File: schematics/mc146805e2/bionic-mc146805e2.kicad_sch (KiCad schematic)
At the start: 5 parts, among them J1 Bionic-P135, J2 Bionic-P245, U1 MC146805E2P, U3 11AA010-I/TO

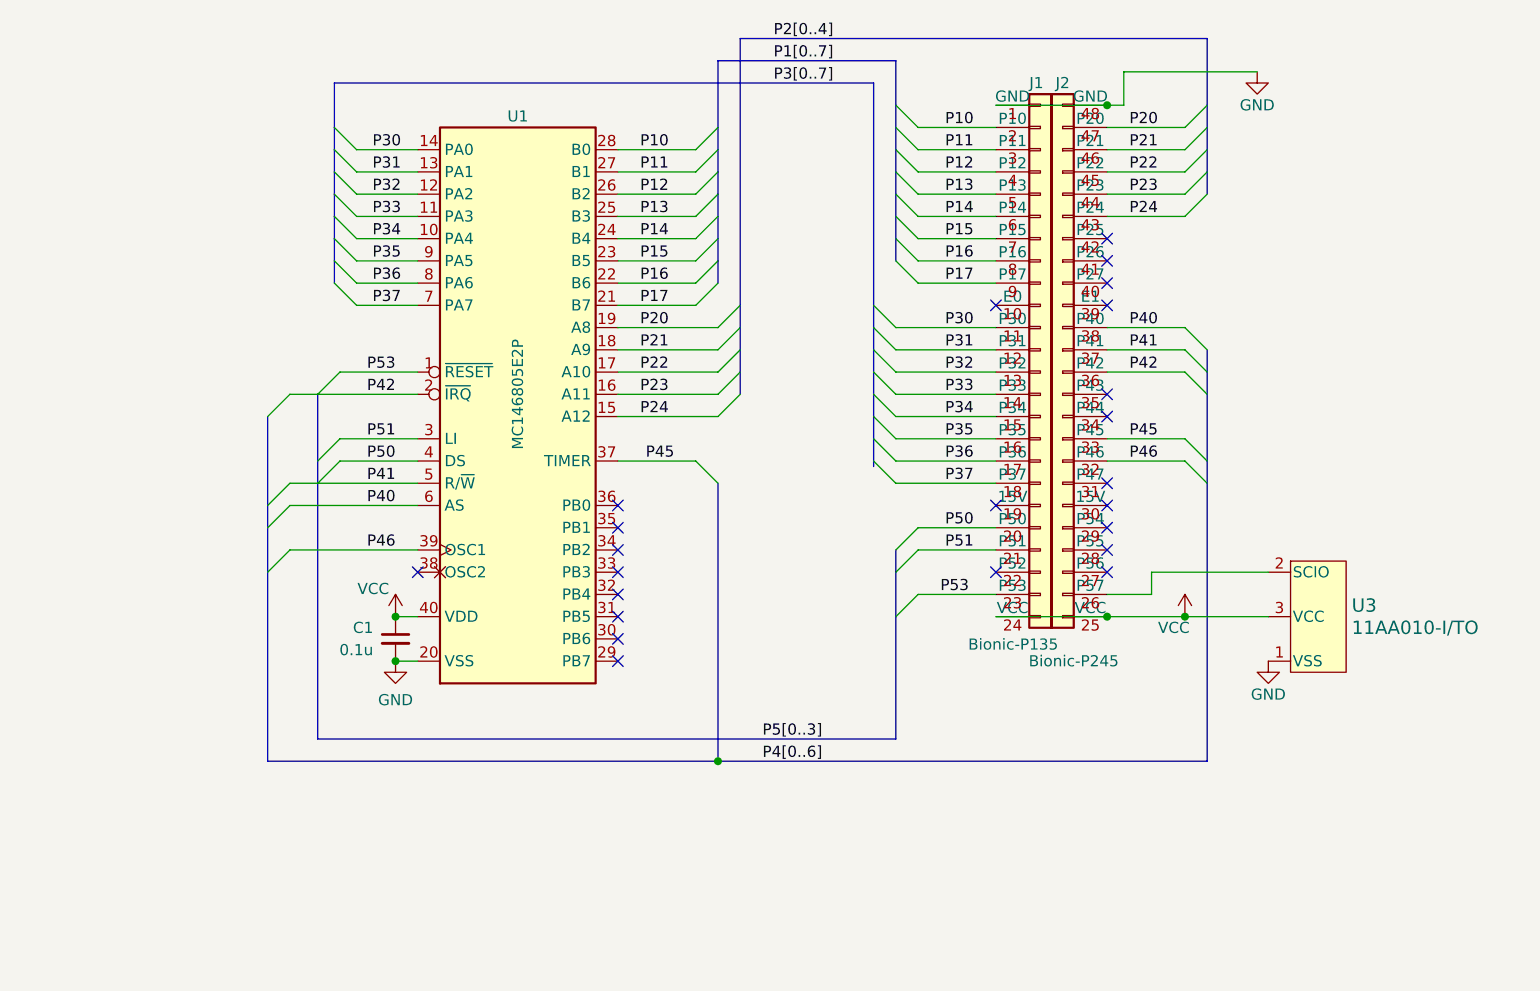
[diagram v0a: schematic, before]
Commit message: [schematics] Make board edges round
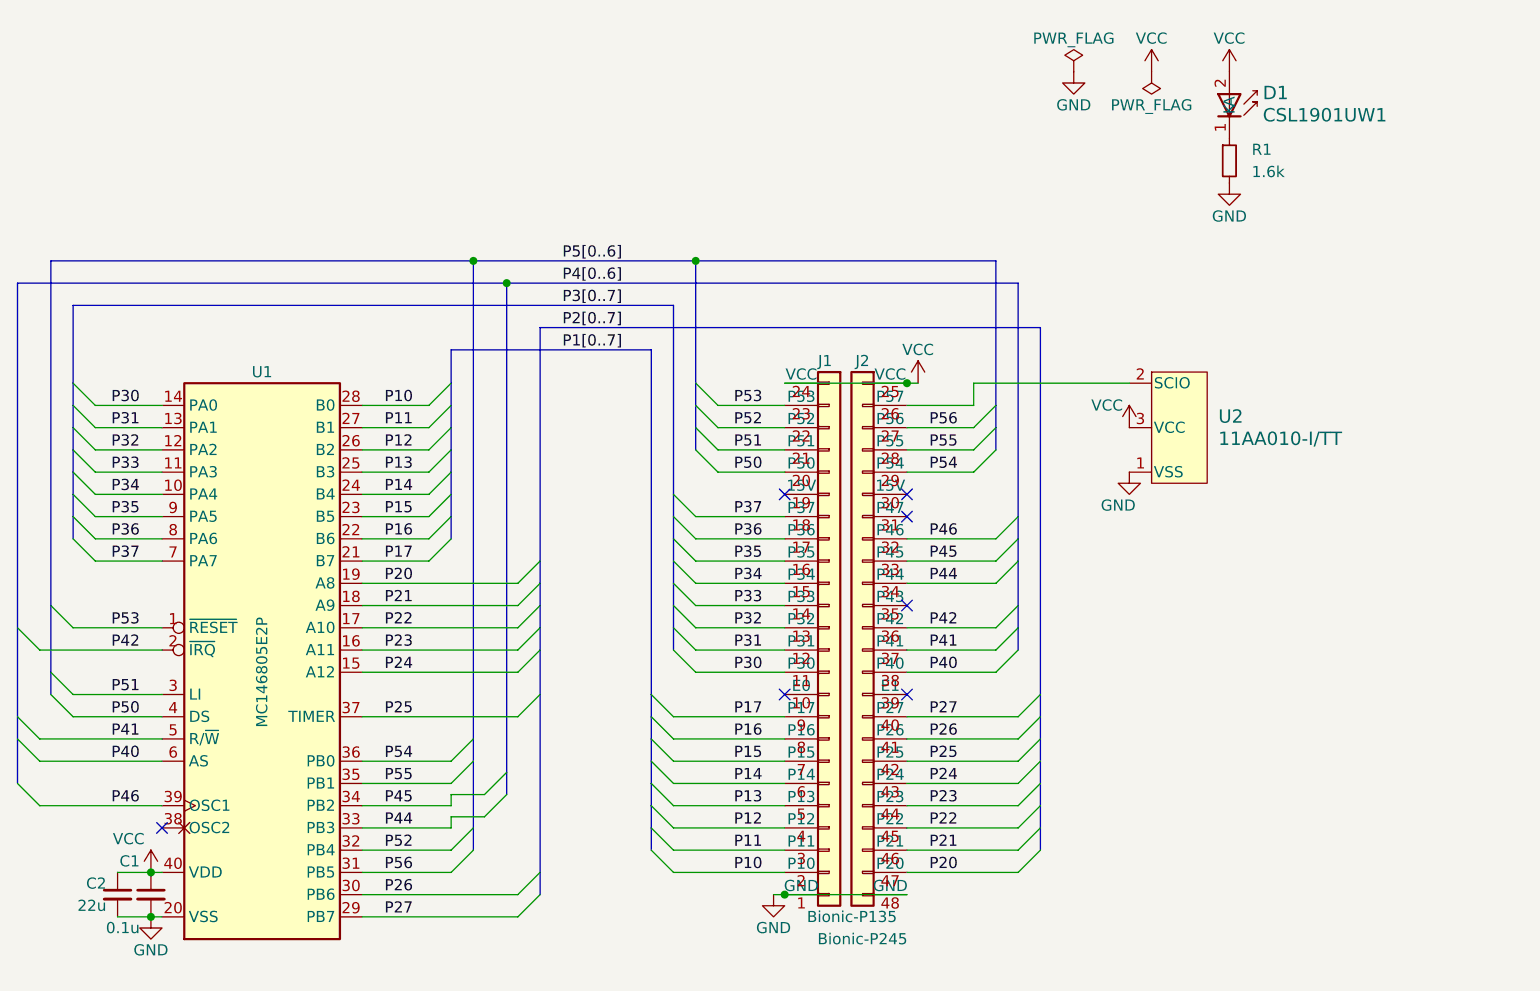
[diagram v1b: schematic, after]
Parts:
- removed U3: 11AA010-I/TO, TO-92_MC_MCH, symbol 0-LocalLibrary:11AA010-I_TO
- added C2: 22u, Capacitor_SMD:C_0603_1608Metric_Pad1.08x0.95mm_HandSolder, symbol Device:C_Small
- added D1: CSL1901UW1, 0-LocalLibrary:LED_CSL1901UW1_ROM, symbol 0-LocalLibrary:CSL1901UW1
- added R1: 1.6k, Resistor_SMD:R_0603_1608Metric_Pad0.98x0.95mm_HandSolder, symbol Device:R_Small
- added U2: 11AA010-I/TT, 0-LocalLibrary:SOT-23_MC_MCH-M, symbol 0-LocalLibrary:11AA010-I_TT
- C1: footprint Capacitor_THT:C_Disc_D3.4mm_W2.1mm_P2.50mm -> Capacitor_SMD:C_0603_1608Metric_Pad1.08x0.95mm_HandSolder
- U1: footprint Package_DIP:DIP-40_W15.24mm -> 0-LocalLibrary:DIP-40_W15.24mm_Socket
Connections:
- net GND: now also C2.2, R1.2, U2.1 (VSS)
- net P45: now also U1.34 (PB2); no longer U1.37 (TIMER)
- net VCC: now also C2.1, D1.2 (A), U2.3 (VCC)
- net P27: now reaches U1.29 (PB7)
- net P27: now also J2.40 (P27)
- net P26: now reaches U1.30 (PB6)
- net P26: now also J2.41 (P26)
- net P56: now reaches U1.31 (PB5)
- net P56: now also J2.27 (P56)
- net P52: now reaches U1.32 (PB4)
- net P52: now also J1.22 (P52)
- net P44: now reaches U1.33 (PB3)
- net P44: now also J2.34 (P44)
- net P55: now reaches U1.35 (PB1)
- net P55: now also J2.28 (P55)
- net P54: now reaches U1.36 (PB0)
- net P54: now also J2.29 (P54)
- net at J2.26 (P57): now also U2.2 (SCIO)
- net P25: now reaches J2.42 (P25)
- net P25: now also U1.37 (TIMER)
- new net: D1.1 (K), R1.1
- no-connect marks 23 -> 7

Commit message: [MC146805E2] Fix EEPROM pinout
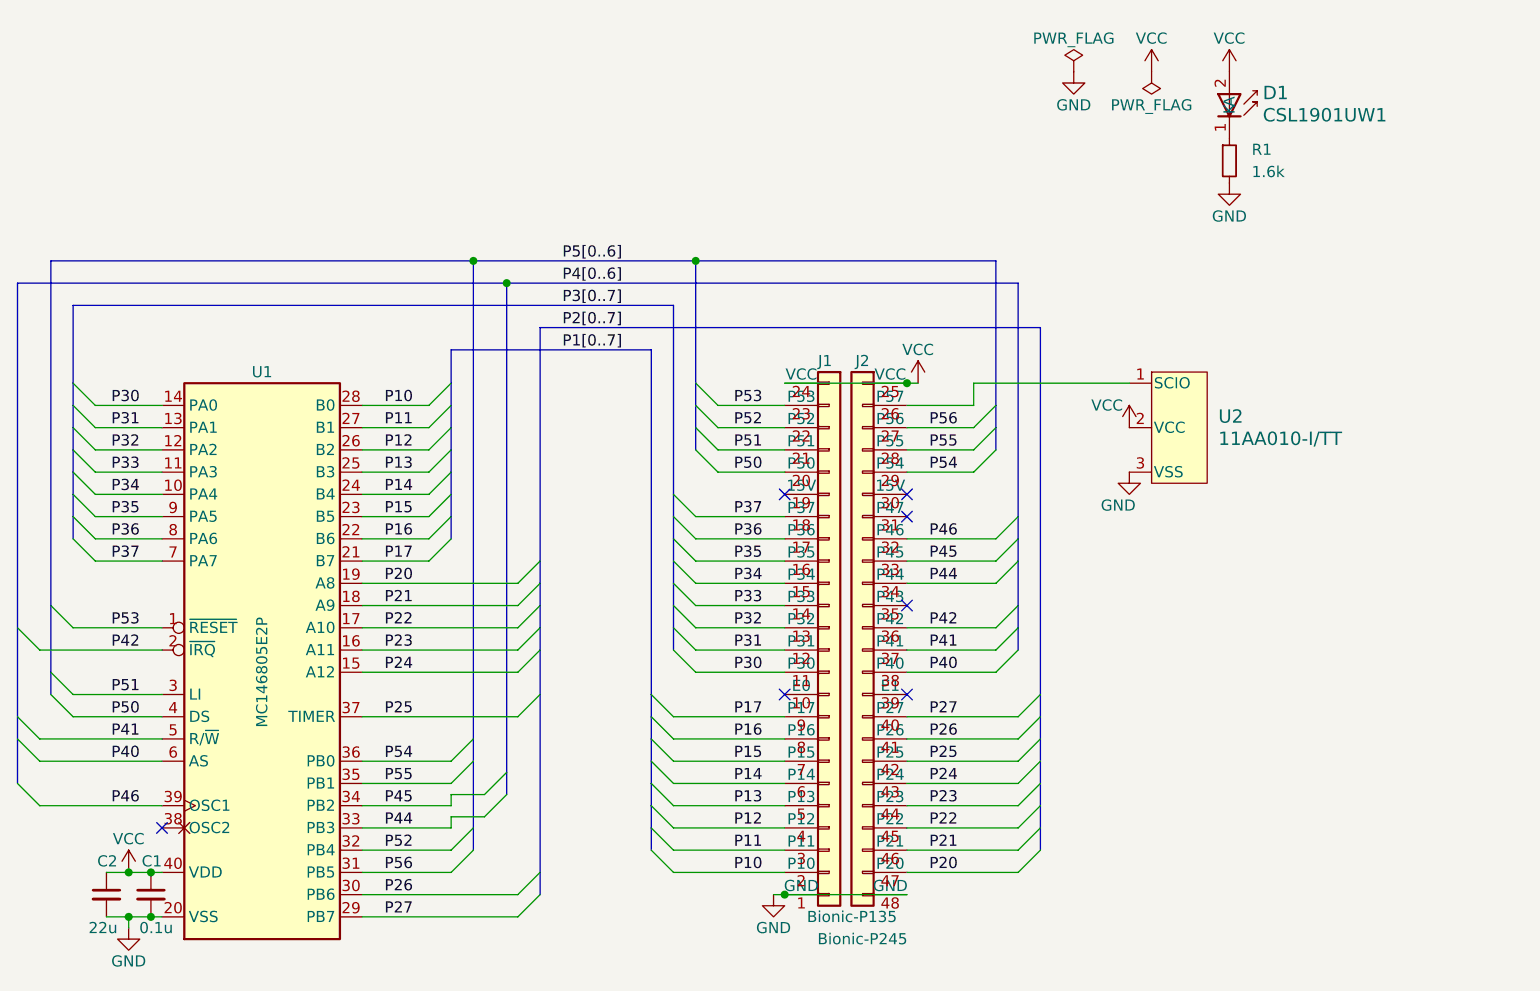
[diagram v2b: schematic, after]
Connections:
- net GND: now also U2.3 (VSS); no longer U2.1 (VSS)
- net VCC: now also U2.2 (VCC); no longer U2.3 (VCC)
- net at J2.26 (P57): now also U2.1 (SCIO); no longer U2.2 (SCIO)
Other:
- moved on the sheet: C2
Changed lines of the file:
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@@
   (title_block
     (title "BionicMC146805E2")
-    (date "2024-10-22")
-    (rev "6")
+    (date "2024-11-01")
+    (rev "7")
     (company "Tadashi G. Takaoka")
   )
   (junction (at 116.84 63.5) (diameter 0) (color 0 0 0 0)
   )
+  (junction (at 77.47 133.35) (diameter 0) (color 0 0 0 0)
+  )
   (junction (at 142.24 63.5) (diameter 0) (color 0 0 0 0)
   )
@@
   )
   (junction (at 80.01 133.35) (diameter 0) (color 0 0 0 0)
+  )
+  (junction (at 77.47 138.43) (diameter 0) (color 0 0 0 0)
   )
   (junction (at 80.01 138.43) (diameter 0) (color 0 0 0 0)
@@
     (stroke (width 0) (type default))
   )
-  (wire (pts (xy 76.2 138.43) (xy 80.01 138.43))
+  (wire (pts (xy 74.93 138.43) (xy 77.47 138.43))
     (stroke (width 0) (type default))
   )
@@
     (stroke (width 0) (type default))
   )
+  (wire (pts (xy 77.47 138.43) (xy 80.01 138.43))
+    (stroke (width 0) (type default))
+  )
   (bus (pts (xy 64.77 66.04) (xy 120.65 66.04))
     (stroke (width 0) (type default))
@@
     (stroke (width 0) (type default))
   )
-  (wire (pts (xy 76.2 133.35) (xy 80.01 133.35))
+  (wire (pts (xy 74.93 133.35) (xy 77.47 133.35))
     (stroke (width 0) (type default))
   )
@@
     (stroke (width 0) (type default))
   )
+  (wire (pts (xy 77.47 133.35) (xy 80.01 133.35))
+    (stroke (width 0) (type default))
+  )
   (wire (pts (xy 67.31 118.11) (xy 81.28 118.11))
     (stroke (width 0) (type default))
@@
   )
   (wire (pts (xy 152.4 77.47) (xy 166.37 77.47))
+    (stroke (width 0) (type default))
+  )
+  (wire (pts (xy 77.47 139.7) (xy 77.47 138.43))
     (stroke (width 0) (type default))
   )
@@
     )
   )
-  (symbol (lib_id "Device:C_Small") (at 76.2 135.89 0) (unit 1)
+  (symbol (lib_id "Device:C_Small") (at 74.93 135.89 0) (unit 1)
     (in_bom yes) (on_board yes) (dnp no)
-    (property "Reference" "C2" (at 74.93 134.62 0)
+    (property "Reference" "C2" (at 76.2 132.08 0)
       (effects (font (size 1.27 1.27)) (justify right))
     )
-    (property "Value" "22u" (at 74.93 137.16 0)
+    (property "Value" "22u" (at 76.2 139.7 0)
       (effects (font (size 1.27 1.27)) (justify right))
     )
-    (property "Footprint" "Capacitor_SMD:C_0603_1608Metric_Pad1.08x0.95mm_HandSolder" (at 76.2 135.89 0)
-      (effects (font (size 1.27 1.27)) hide)
-    )
-    (property "Datasheet" "~" (at 76.2 135.89 0)
+    (property "Footprint" "Capacitor_SMD:C_0603_1608Metric_Pad1.08x0.95mm_HandSolder" (at 74.93 135.89 0)
+      (effects (font (size 1.27 1.27)) hide)
+    )
+    (property "Datasheet" "~" (at 74.93 135.89 0)
       (effects (font (size 1.27 1.27)) hide)
     )
@@
     )
   )
-  (symbol (lib_id "power:VCC") (at 80.01 133.35 0) (unit 1)
+  (symbol (lib_id "power:VCC") (at 77.47 133.35 0) (unit 1)
     (in_bom yes) (on_board yes) (dnp no)
-    (property "Reference" "#PWR04" (at 80.01 137.16 0)
+    (property "Reference" "#PWR04" (at 77.47 137.16 0)
       (effects (font (size 1.27 1.27)) hide)
     )
@@
       (effects (font (size 1.27 1.27)))
     )
-    (property "Footprint" "" (at 80.01 133.35 0)
-      (effects (font (size 1.27 1.27)) hide)
-    )
-    (property "Datasheet" "" (at 80.01 133.35 0)
+    (property "Footprint" "" (at 77.47 133.35 0)
+      (effects (font (size 1.27 1.27)) hide)
+    )
+    (property "Datasheet" "" (at 77.47 133.35 0)
       (effects (font (size 1.27 1.27)) hide)
     )
@@
     )
   )
-  (symbol (lib_id "power:GND") (at 80.01 138.43 0) (unit 1)
+  (symbol (lib_id "power:GND") (at 77.47 139.7 0) (unit 1)
     (in_bom yes) (on_board yes) (dnp no)
-    (property "Reference" "#PWR03" (at 80.01 144.78 0)
-      (effects (font (size 1.27 1.27)) hide)
-    )
-    (property "Value" "GND" (at 80.01 142.24 0)
+    (property "Reference" "#PWR03" (at 77.47 146.05 0)
+      (effects (font (size 1.27 1.27)) hide)
+    )
+    (property "Value" "GND" (at 77.47 143.51 0)
       (effects (font (size 1.27 1.27)))
     )
-    (property "Footprint" "" (at 80.01 138.43 0)
-      (effects (font (size 1.27 1.27)) hide)
-    )
-    (property "Datasheet" "" (at 80.01 138.43 0)
+    (property "Footprint" "" (at 77.47 139.7 0)
+      (effects (font (size 1.27 1.27)) hide)
+    )
+    (property "Datasheet" "" (at 77.47 139.7 0)
       (effects (font (size 1.27 1.27)) hide)
     )
@@
   (symbol (lib_id "Device:C_Small") (at 80.01 135.89 0) (unit 1)
     (in_bom yes) (on_board yes) (dnp no)
-    (property "Reference" "C1" (at 78.74 132.08 0)
+    (property "Reference" "C1" (at 81.28 132.08 0)
       (effects (font (size 1.27 1.27)) (justify right))
     )
-    (property "Value" "0.1u" (at 78.74 139.7 0)
+    (property "Value" "0.1u" (at 82.55 139.7 0)
       (effects (font (size 1.27 1.27)) (justify right))
     )

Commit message: [MC146805E2] Shrink board size
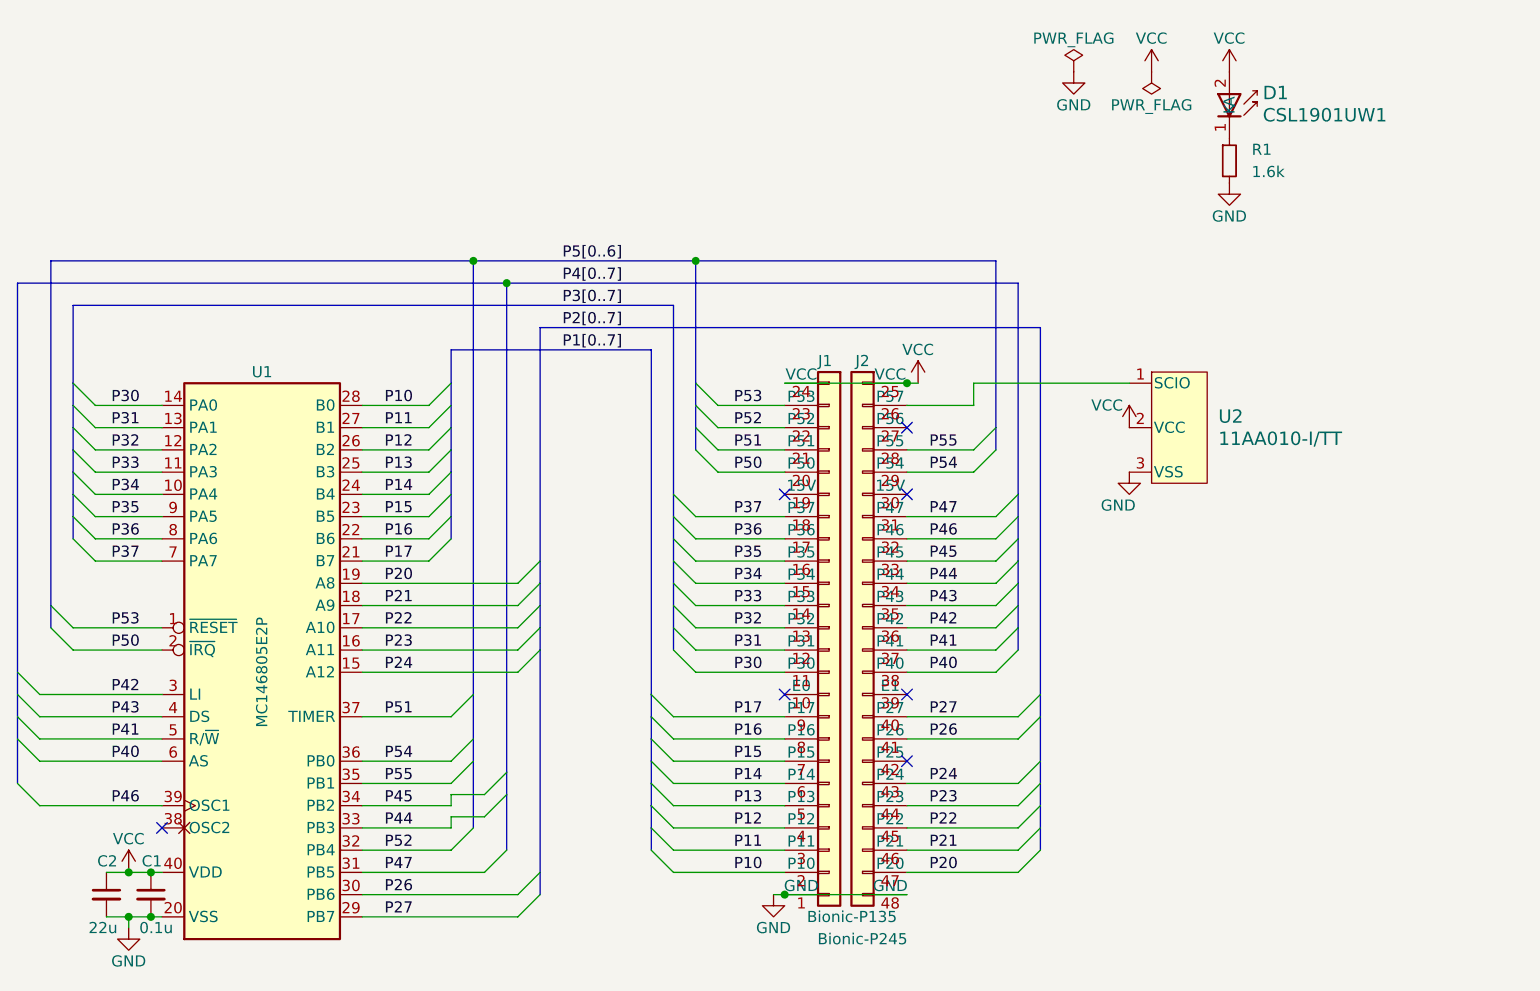
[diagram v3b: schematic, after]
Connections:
- net P42: now also U1.3 (LI); no longer U1.2 (~{IRQ})
- net P50: now also U1.2 (~{IRQ}); no longer U1.4 (DS)
- net P51: now also U1.37 (TIMER); no longer U1.3 (LI)
- net P47: now reaches J2.31 (P47)
- net P47: now also U1.31 (PB5)
- net P43: now reaches J2.35 (P43)
- net P43: now also U1.4 (DS)
- net P25: no longer names the net of J2.42 (P25)
- net P25: no longer U1.37 (TIMER)
- net P56: no longer names the net of J2.27 (P56)
- net P56: no longer U1.31 (PB5)

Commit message: [schematics] Update LED footprint
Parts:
- D1: footprint 0-LocalLibrary:LED_CSL1901UW1_ROM -> 0-LocalLibrary:LED_CSL1901UW1_ROM-M
- J1: footprint connector:Bionic-P135_Vertical -> 0-LocalLibrary:Bionic-P135_Vertical
- J2: footprint connector:Bionic-P245_Vertical -> 0-LocalLibrary:Bionic-P245_Vertical
